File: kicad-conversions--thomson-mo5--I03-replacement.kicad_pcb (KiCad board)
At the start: 2 copper layers, 3 parts, among them U1 HM7603_32×8_PROM_THREE-STATE_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, U2 HIGH_PERFORMANCE_E2_CMOS_PLD_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

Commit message: done wiring
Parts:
- moved C1 13.6 mm to (78.1, 72.4), turned to 180 degrees
- moved U2 7.10 mm to (73.0, 74.9)
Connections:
- net Net-(U1-GND) renamed /GND
- net Net-(U1-VCC) renamed /VCC
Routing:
- net /~{CE}: track 0.00 -> 25.3 mm, vias 0 -> 1
- net /A1: track 0.00 -> 11.3 mm
- net /A4: track 0.00 -> 11.3 mm
- net /A3: track 0.00 -> 11.3 mm
- net /A2: track 0.00 -> 11.3 mm
- net /A0: track 0.00 -> 11.3 mm
- net /VCC: track 0.00 -> 6.24 mm
- net /GND: track 0.00 -> 6.13 mm
- net /O4: track 0.00 -> 4.97 mm
- net /O2: track 0.00 -> 4.97 mm
- net /O7: track 0.00 -> 4.97 mm
- net /O6: track 0.00 -> 4.97 mm
- net /O5: track 0.00 -> 4.97 mm
- net /O3: track 0.00 -> 4.97 mm
- net /O1: track 0.00 -> 4.97 mm
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- added copper zone on B.Cu, net /GND
- added copper zone on F.Cu, net /GND
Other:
- board outline added: 15.9 x 29.8 mm

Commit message: final adjustments
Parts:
- added G***: LOGO, cliparts:logo--cc--cc, F.Cu at (76.8, 97.8)
- added G***: LOGO, cliparts:logo--cc--zero, F.Cu at (83.8, 97.8)
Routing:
- net /GND: track 6.13 -> 14.9 mm

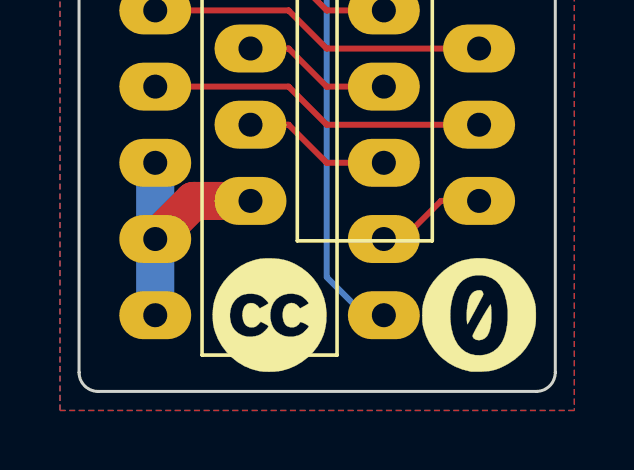
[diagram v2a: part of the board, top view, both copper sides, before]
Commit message: schematic -- rename wires with functionnal names
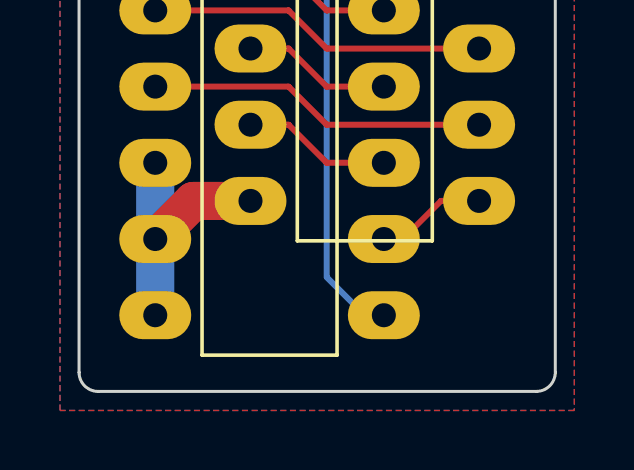
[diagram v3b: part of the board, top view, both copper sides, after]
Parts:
- removed G***: LOGO, cliparts:logo--cc--cc
- removed G***: LOGO, cliparts:logo--cc--zero
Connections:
- net /A0 renamed /ROUGE
- net /A1 renamed /VERT
- net /A2 renamed /BLEU
- net /A3 renamed /PASTEL
- net /A4 renamed /~{SUPLT}
- net /O1 renamed /R1
- net /O2 renamed /R2
- net /O3 renamed /V1
- net /O4 renamed /V2
- net /O5 renamed /B1
- net /O6 renamed /B2
- net /O8 renamed /~{NOIR_INCR}

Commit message: added proper description in schematic, pcb
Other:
- board text added: "${COMMENT1}"
- board text added: "CC0"
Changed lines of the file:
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@@
   (paper "A4" portrait)
   (title_block
+    (title "Replacement of I03 (color PROM) for the Thomson MO5")
     (date "2024-11-03")
+    (rev "v1.0.0-beta")
+    (company "Sporniket")
+    (comment 1 "#1")
+    (comment 3 "https://github.com/sporniket/kicad-conversions--thomson-mo5--i03-replacement")
+    (comment 4 "Original repository :")
   )
   (layers
@@
   (gr_line (start 86.36 71.12) (end 86.36 99.695)
     (stroke (width 0.1) (type default)) (layer "Edge.Cuts"))
+  (gr_text "CC0" (at 76.835 97.155) (layer "B.SilkS" knockout)
+    (effects (font (size 1.5 1.5) (thickness 0.3) bold) (justify bottom mirror))
+  )
+  (gr_text "${COMMENT1}" (at 76.835 99.187) (layer "B.SilkS")
+    (effects (font (size 1.5 1.5) (thickness 0.1875)) (justify bottom mirror))
+  )
   (segment (start 77.47 76.2) (end 76.2 76.2) (width 0.2) (layer "F.Cu") (net 1))
   (segment (start 78.74 77.47) (end 77.47 76.2) (width 0.2) (layer "F.Cu") (net 1))
